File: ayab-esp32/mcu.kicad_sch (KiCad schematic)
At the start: 26 parts, among them Q201 AO3400A, SW201 USER, SW202 RESET, SW203 BOOTSEL, U201 ESP32-S3-MINI-1

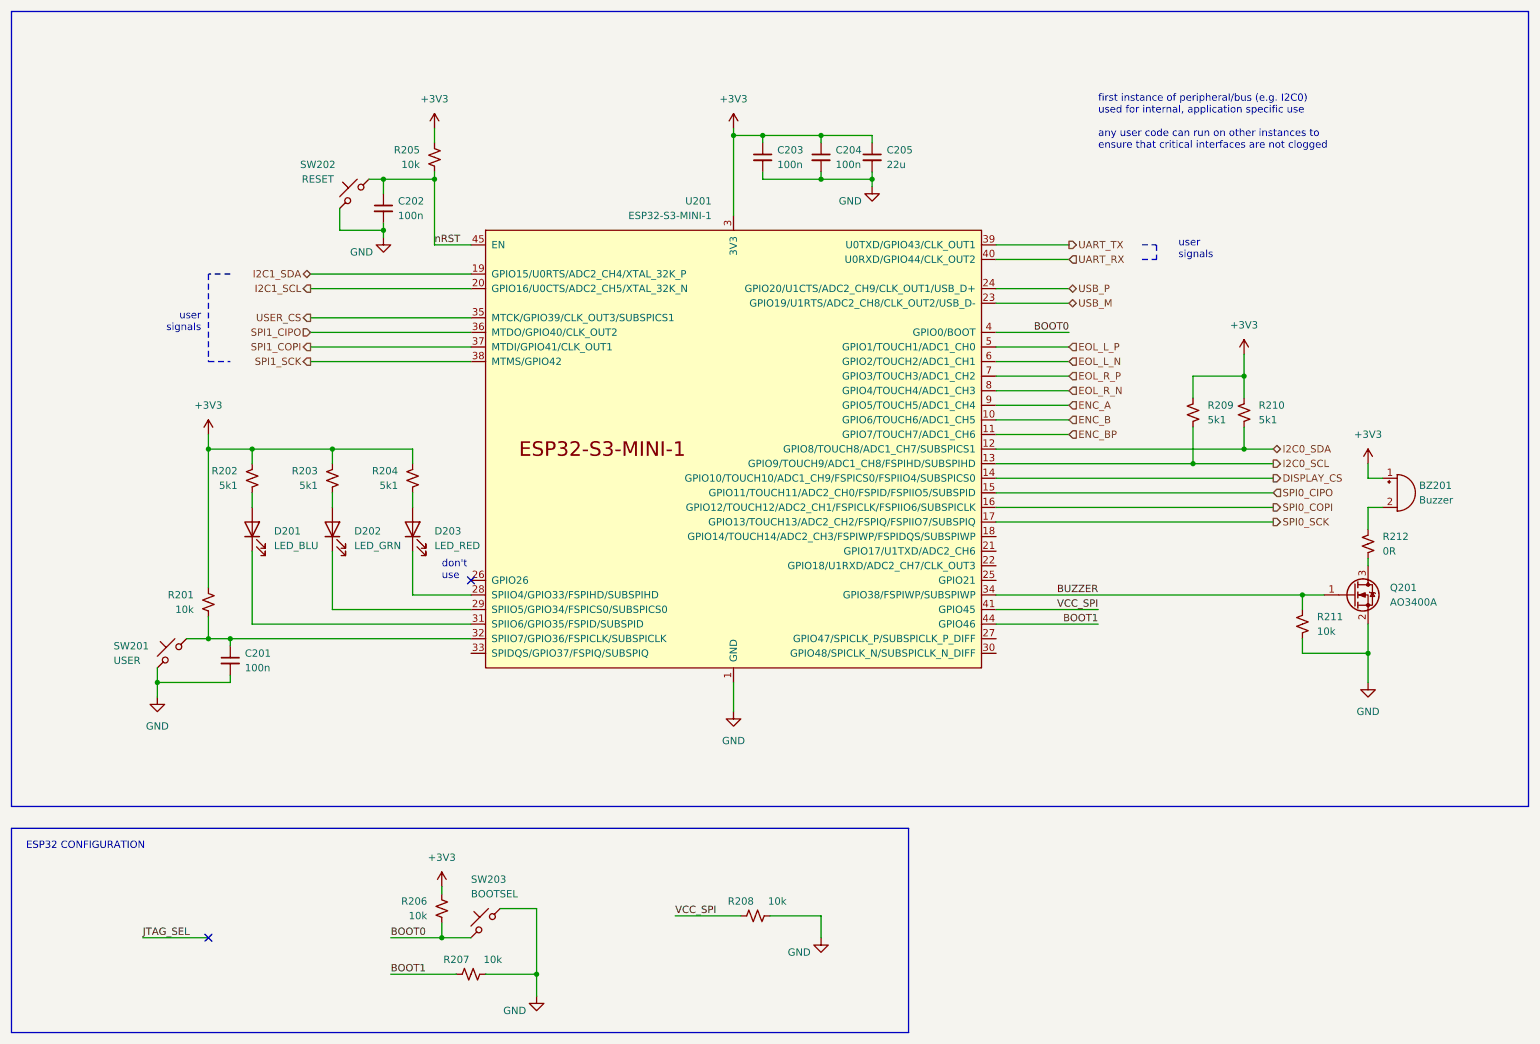
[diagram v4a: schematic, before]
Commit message: add component selection, bom
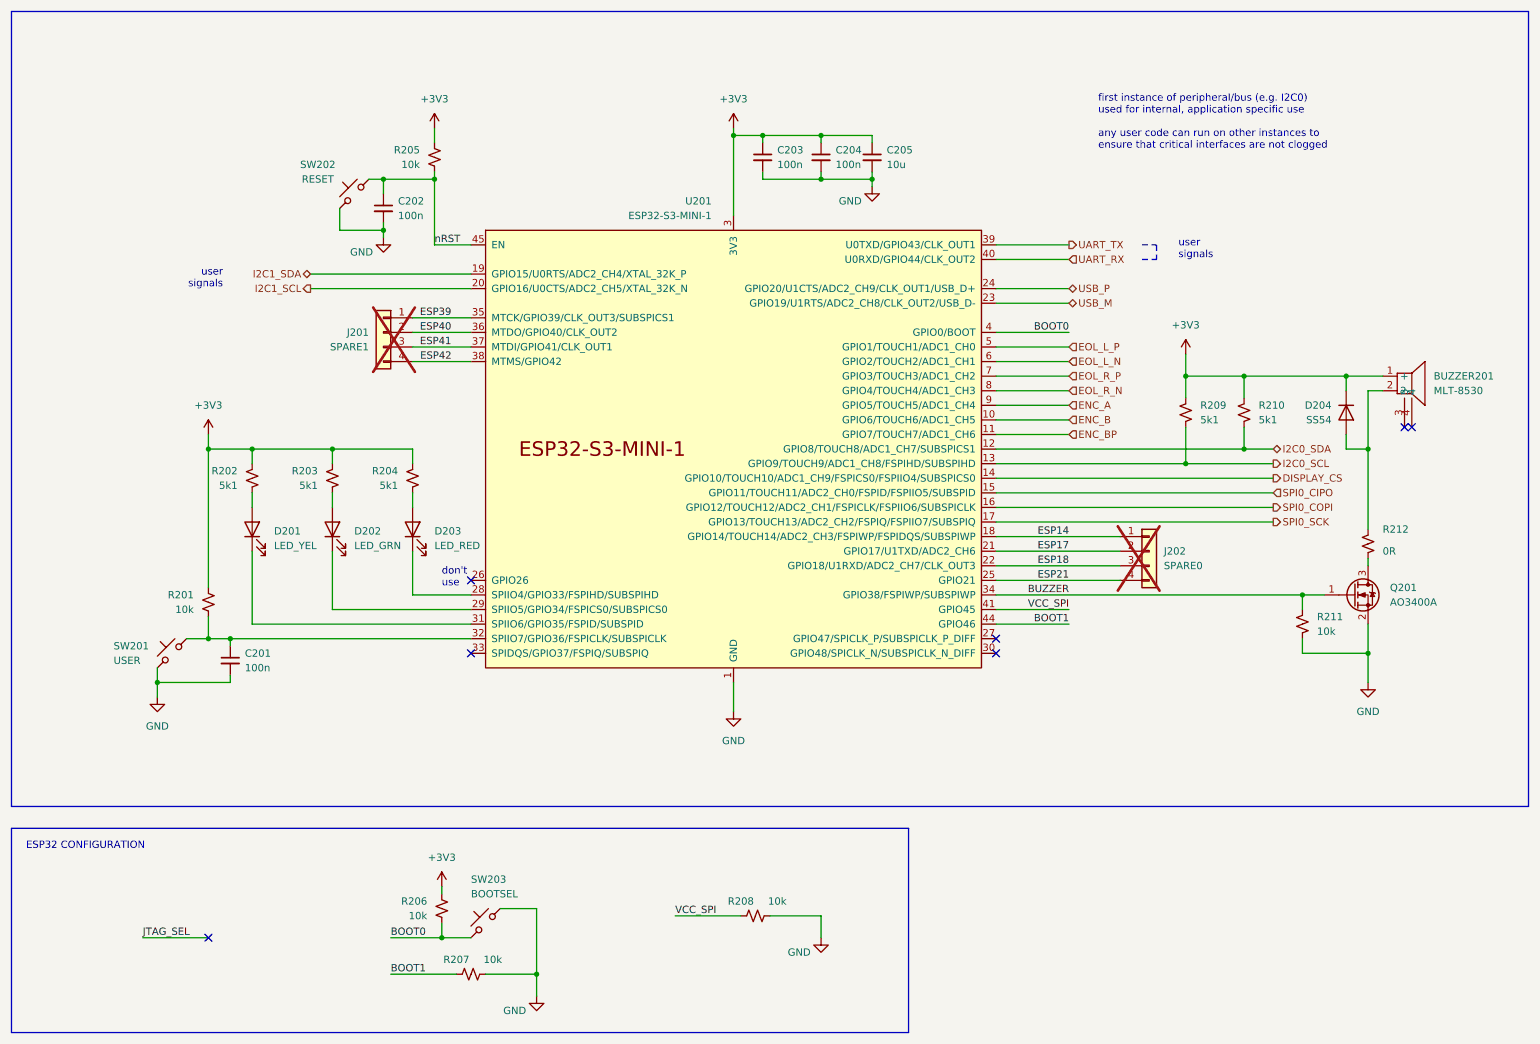
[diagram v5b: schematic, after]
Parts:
- removed BZ201: Buzzer, symbol ayab-esp32:Buzzer
- added BUZZER201: MLT-8530, Library:BUZ-SMD_4P-L8.5-W8.5-P8.50-BR, symbol Library:MLT-8530
- added D204: SS54, Diode_SMD:D_SMA, symbol Library:D
- added J201: SPARE1, Connector_PinSocket_2.54mm:PinSocket_1x04_P2.54mm_Vertical, symbol Library:Conn_01x04
- added J202: SPARE0, Connector_PinSocket_2.54mm:PinSocket_1x04_P2.54mm_Vertical, symbol Library:Conn_01x04
- C201, C202, C203, C204: footprint (none) -> Capacitor_SMD:C_0603_1608Metric; symbol ayab-esp32:C_Small -> Library:C_Small; LCSC ID (none) -> C57112; OEM (none) -> FH (Guangdong Fenghua Advanced Tech); OEM PN (none) -> 0603B103K500NT; Package (none) -> 0603; Voltage rating (none) -> 24V X7R
- C205: value 22u -> 10u; footprint (none) -> Capacitor_SMD:C_0805_2012Metric; symbol ayab-esp32:C_Small -> Library:C_Small; LCSC ID (none) -> C15850; OEM (none) -> Samsung Electro-Mechanics; OEM PN (none) -> CL21A106KAYNNNE; Package (none) -> 0805; Voltage rating (none) -> 24V X5R
- D201: value LED_BLU -> LED_YEL; footprint (none) -> Diode_SMD:D_0805_2012Metric; symbol ayab-esp32:LED -> Library:LED; LCSC ID (none) -> C2296; OEM (none) -> Hubei KENTO Elec; OEM PN (none) -> C2296; Package (none) -> 0805
- D202: footprint (none) -> Diode_SMD:D_0805_2012Metric; symbol ayab-esp32:LED -> Library:LED; LCSC ID (none) -> C2297; OEM (none) -> Hubei KENTO Elec; OEM PN (none) -> C2297; Package (none) -> 0805
- D203: footprint (none) -> Diode_SMD:D_0805_2012Metric; symbol ayab-esp32:LED -> Library:LED; LCSC ID (none) -> C84256; OEM (none) -> Foshan NationStar Optoelectronics; OEM PN (none) -> NCD0805R1; Package (none) -> 0805
- Q201: symbol ayab-esp32:AO3400A -> Library:AO3400A; LCSC ID (none) -> C20917; OEM (none) -> Alpha & Omega Semicon; OEM PN (none) -> AO3400A; Package (none) -> SOT-23
- R201, R205, R206, R207, R208, R211: footprint (none) -> Resistor_SMD:R_0603_1608Metric; symbol ayab-esp32:R_Small_US -> Library:R_Small_US; LCSC ID (none) -> C25804; OEM (none) -> UNI-ROYAL(Uniroyal Elec); OEM PN (none) -> 0603WAF1002T5E; Package (none) -> 0603
- R202, R203, R204, R209, R210: footprint (none) -> Resistor_SMD:R_0603_1608Metric; symbol ayab-esp32:R_Small_US -> Library:R_Small_US; LCSC ID (none) -> C23186; OEM (none) -> UNI-ROYAL(Uniroyal Elec); OEM PN (none) -> 0603WAF5101T5E; Package (none) -> 0603
- R212: footprint (none) -> Resistor_SMD:R_0603_1608Metric; symbol ayab-esp32:R_Small_US -> Library:R_Small_US; LCSC ID (none) -> C21189; OEM (none) -> UNI-ROYAL(Uniroyal Elec); OEM PN (none) -> 0603WAF0000T5E; Package (none) -> 0603
- SW201, SW202, SW203: footprint (none) -> matei:TS-1187A-B-A-B; symbol ayab-esp32:SW_Push_45deg -> Library:SW_Push_45deg; LCSC ID (none) -> C318884; OEM (none) -> XKB Connectivity; OEM PN (none) -> TS-1187A-B-A-B; Package (none) -> TS-1187ABAB
- U201: symbol ayab-esp32:ESP32-S3-MINI-1 -> Library:ESP32-S3-MINI-1; LCSC ID (none) -> C3013941; OEM (none) -> Espressif Systems; OEM PN (none) -> ESP32-S3-MINI-1-N4R2; Package (none) -> SMD
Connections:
- net +3V3: now also BUZZER201.1 (+), D204.1 (K)
- net ESP14: now reaches U201.18 (GPIO14/TOUCH14/ADC2_CH3/FSPIWP/FSPIDQS/SUBSPIWP)
- net ESP14: now also J202.1 (Pin_1)
- net ESP17: now reaches U201.21 (GPIO17/U1TXD/ADC2_CH6)
- net ESP17: now also J202.2 (Pin_2)
- net ESP18: now reaches U201.22 (GPIO18/U1RXD/ADC2_CH7/CLK_OUT3)
- net ESP18: now also J202.3 (Pin_3)
- net ESP21: now reaches U201.25 (GPIO21)
- net ESP21: now also J202.4 (Pin_4)
- net at R212.1: now also BUZZER201.2, D204.2 (A)
- net SPI1_CIPO renamed ESP40
- net ESP40: now also J201.2 (Pin_2)
- net SPI1_COPI renamed ESP41
- net ESP41: now also J201.3 (Pin_3)
- net SPI1_SCK renamed ESP42
- net ESP42: now also J201.4 (Pin_4)
- net USER_CS renamed ESP39
- net ESP39: now also J201.1 (Pin_1)
- no-connect marks 2 -> 7
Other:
- moved on the sheet: R209

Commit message: review ZVD P-ch MOSFET and resistors
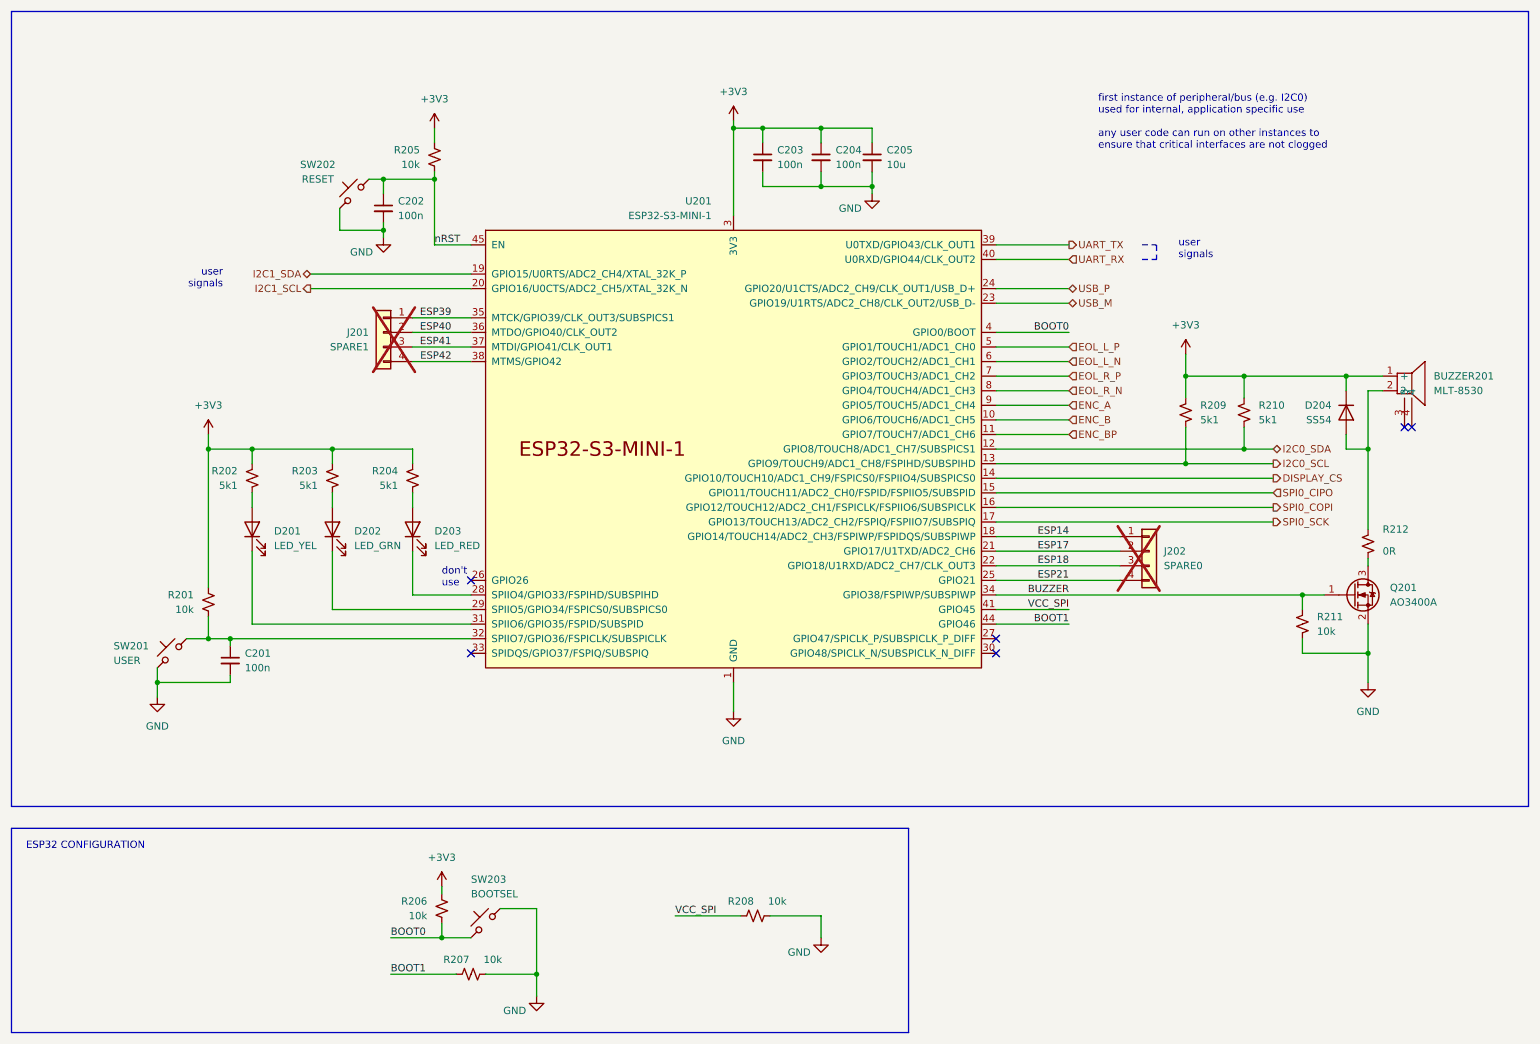
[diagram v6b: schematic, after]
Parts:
- BUZZER201: footprint Library:BUZ-SMD_4P-L8.5-W8.5-P8.50-BR -> easyeda2kicad:BUZ-SMD_4P-L8.5-W8.5-P8.50-BR; symbol Library:MLT-8530 -> ayab-lib:MLT-8530
- C201, C202, C203, C204, C205: symbol Library:C_Small -> ayab-lib:C_Small
- D201, D202, D203: symbol Library:LED -> ayab-lib:LED
- D204: symbol Library:D -> ayab-lib:D
- J201, J202: symbol Library:Conn_01x04 -> ayab-lib:Conn_01x04
- Q201: symbol Library:AO3400A -> ayab-lib:AO3400A
- R201, R202, R203, R204, R205, R206, R207, R208, R209, R210, R211, R212: symbol Library:R_Small_US -> ayab-lib:R_Small_US
- SW201, SW202, SW203: symbol Library:SW_Push_45deg -> ayab-lib:SW_Push_45deg
- U201: symbol Library:ESP32-S3-MINI-1 -> ayab-lib:ESP32-S3-MINI-1
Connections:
- no-connect marks 7 -> 6

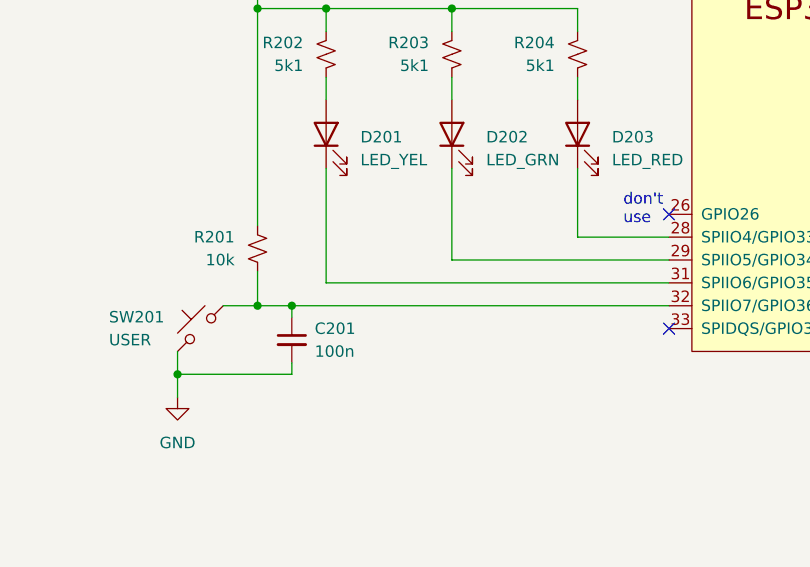
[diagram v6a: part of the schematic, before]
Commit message: first draft layout DRC clean
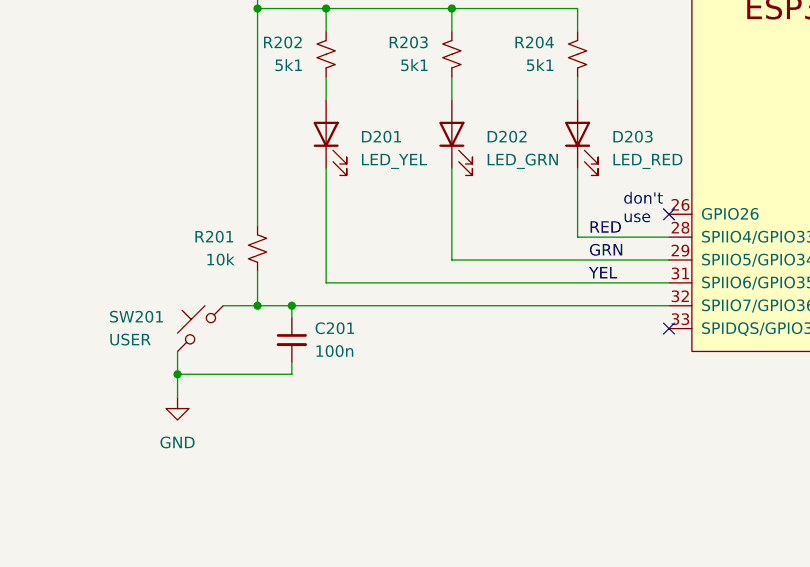
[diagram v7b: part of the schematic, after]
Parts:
- J201, J202: footprint Connector_PinSocket_2.54mm:PinSocket_1x04_P2.54mm_Vertical -> Connector_PinHeader_2.54mm:PinHeader_1x04_P2.54mm_Horizontal
- SW201, SW202, SW203: footprint matei:TS-1187A-B-A-B -> easyeda2kicad:KEY-TH_4P-L7.5-W11.5-P4.5; LCSC ID C318884 -> C2689823; OEM XKB Connectivity -> Yuandi; OEM PN TS-1187A-B-A-B -> TS-1093C-A145B3-D1
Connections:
- net GND: now also SW201.2; no longer SW201.1
- net RED: now reaches D203.1 (K), U201.28 (SPIIO4/GPIO33/FSPIHD/SUBSPIHD)
- net GRN: now reaches D202.1 (K), U201.29 (SPIIO5/GPIO34/FSPICS0/SUBSPICS0)
- net YEL: now reaches D201.1 (K), U201.31 (SPIIO6/GPIO35/FSPID/SUBSPID)
- net at C201.1, R201.2, U201.32 (SPIIO7/GPIO36/FSPICLK/SUBSPICLK): now also SW201.1; no longer SW201.2
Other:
- moved on the sheet: SW201
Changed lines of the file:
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@@
     (effects (font (size 1.27 1.27)) (justify right bottom))
+  )
+  (label "GRN" (at 87.63 120.65 0) (fields_autoplaced)
+    (effects (font (size 1.27 1.27)) (justify left bottom))
+  )
+  (label "RED" (at 87.63 118.11 0) (fields_autoplaced)
+    (effects (font (size 1.27 1.27)) (justify left bottom))
   )
   (label "ESP39" (at 87.63 69.85 0) (fields_autoplaced)
@@
   (label "BOOT0" (at 200.66 72.39 180) (fields_autoplaced)
     (effects (font (size 1.27 1.27)) (justify right bottom))
+  )
+  (label "YEL" (at 87.63 123.19 0) (fields_autoplaced)
+    (effects (font (size 1.27 1.27)) (justify left bottom))
   )
   (label "ESP17" (at 200.66 110.49 180) (fields_autoplaced)
@@
       (effects (font (size 1.27 1.27)) (justify left))
     )
-    (property "Footprint" "Connector_PinSocket_2.54mm:PinSocket_1x04_P2.54mm_Vertical" (at 81.28 72.39 0)
+    (property "Footprint" "Connector_PinHeader_2.54mm:PinHeader_1x04_P2.54mm_Horizontal" (at 81.28 72.39 0)
       (effects (font (size 1.27 1.27)) hide)
     )
@@
       (effects (font (size 1.27 1.27)) (justify right))
     )
-    (property "Footprint" "matei:TS-1187A-B-A-B" (at 99.06 175.26 0)
+    (property "Footprint" "easyeda2kicad:KEY-TH_4P-L7.5-W11.5-P4.5" (at 99.06 175.26 0)
       (effects (font (size 1.27 1.27)) hide)
     )
@@
       (effects (font (size 1.27 1.27)) hide)
     )
-    (property "LCSC ID" "C318884" (at 99.06 175.26 0)
+    (property "LCSC ID" "C2689823" (at 99.06 175.26 0)
       (effects (font (size 1.27 1.27)) hide)
     )
@@
       (effects (font (size 1.27 1.27)) hide)
     )
-    (property "OEM PN" "TS-1187A-B-A-B" (at 99.06 175.26 0)
-      (effects (font (size 1.27 1.27)) hide)
-    )
-    (property "OEM" "XKB Connectivity" (at 99.06 175.26 0)
+    (property "OEM PN" "TS-1093C-A145B3-D1" (at 99.06 175.26 0)
+      (effects (font (size 1.27 1.27)) hide)
+    )
+    (property "OEM" "Yuandi" (at 99.06 175.26 0)
       (effects (font (size 1.27 1.27)) hide)
     )
@@
       (effects (font (size 1.27 1.27)))
     )
-    (property "Footprint" "matei:TS-1187A-B-A-B" (at 76.2 48.26 0)
+    (property "Footprint" "easyeda2kicad:KEY-TH_4P-L7.5-W11.5-P4.5" (at 76.2 48.26 0)
       (effects (font (size 1.27 1.27)) hide)
     )
@@
       (effects (font (size 1.27 1.27)) hide)
     )
-    (property "LCSC ID" "C318884" (at 76.2 48.26 0)
+    (property "LCSC ID" "C2689823" (at 76.2 48.26 0)
       (effects (font (size 1.27 1.27)) hide)
     )
@@
       (effects (font (size 1.27 1.27)) hide)
     )
-    (property "OEM PN" "TS-1187A-B-A-B" (at 76.2 48.26 0)
-      (effects (font (size 1.27 1.27)) hide)
-    )
-    (property "OEM" "XKB Connectivity" (at 76.2 48.26 0)
+    (property "OEM PN" "TS-1093C-A145B3-D1" (at 76.2 48.26 0)
+      (effects (font (size 1.27 1.27)) hide)
+    )
+    (property "OEM" "Yuandi" (at 76.2 48.26 0)
       (effects (font (size 1.27 1.27)) hide)
     )
@@
     )
   )
-  (symbol (lib_id "ayab-lib:SW_Push_45deg") (at 44.45 128.27 90) (unit 1)
-    (in_bom yes) (on_board yes) (dnp no)
-    (property "Reference" "SW201" (at 34.29 127 90)
-      (effects (font (size 1.27 1.27)) (justify right))
-    )
-    (property "Value" "USER" (at 34.29 129.54 90)
-      (effects (font (size 1.27 1.27)) (justify right))
-    )
-    (property "Footprint" "matei:TS-1187A-B-A-B" (at 44.45 128.27 0)
+  (symbol (lib_id "ayab-lib:SW_Push_45deg") (at 44.45 128.27 0) (mirror y) (unit 1)
+    (in_bom yes) (on_board yes) (dnp no)
+    (property "Reference" "SW201" (at 34.29 127 0)
+      (effects (font (size 1.27 1.27)) (justify right))
+    )
+    (property "Value" "USER" (at 34.29 129.54 0)
+      (effects (font (size 1.27 1.27)) (justify right))
+    )
+    (property "Footprint" "easyeda2kicad:KEY-TH_4P-L7.5-W11.5-P4.5" (at 44.45 128.27 0)
       (effects (font (size 1.27 1.27)) hide)
     )
@@
       (effects (font (size 1.27 1.27)) hide)
     )
-    (property "LCSC ID" "C318884" (at 44.45 128.27 0)
+    (property "LCSC ID" "C2689823" (at 44.45 128.27 0)
       (effects (font (size 1.27 1.27)) hide)
     )
@@
       (effects (font (size 1.27 1.27)) hide)
     )
-    (property "OEM PN" "TS-1187A-B-A-B" (at 44.45 128.27 0)
-      (effects (font (size 1.27 1.27)) hide)
-    )
-    (property "OEM" "XKB Connectivity" (at 44.45 128.27 0)
+    (property "OEM PN" "TS-1093C-A145B3-D1" (at 44.45 128.27 0)
+      (effects (font (size 1.27 1.27)) hide)
+    )
+    (property "OEM" "Yuandi" (at 44.45 128.27 0)
       (effects (font (size 1.27 1.27)) hide)
     )
@@
       (effects (font (size 1.27 1.27)) (justify left))
     )
-    (property "Footprint" "Connector_PinSocket_2.54mm:PinSocket_1x04_P2.54mm_Vertical" (at 214.63 110.49 0)
-      (effects (font (size 1.27 1.27)) hide)
-    )
+    (property "Footprint" "Connector_PinHeader_2.54mm:PinHeader_1x04_P2.54mm_Horizontal" (at 214.63 110.49 0)
+      (effects (font (size 1.27 1.27)) hide)
+    )
